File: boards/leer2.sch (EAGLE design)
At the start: 61 parts, among them IC1 XMEGA128A1, IC2 7805DT, Q1 BC846BSMD, Q2 BC846BSMD, Q3 BC846BSMD, Q4 BC846BSMD, Q5 BC846BSMD, Q6 BC846BSMD, Q7 BC846BSMD, Q8 BC846BSMD

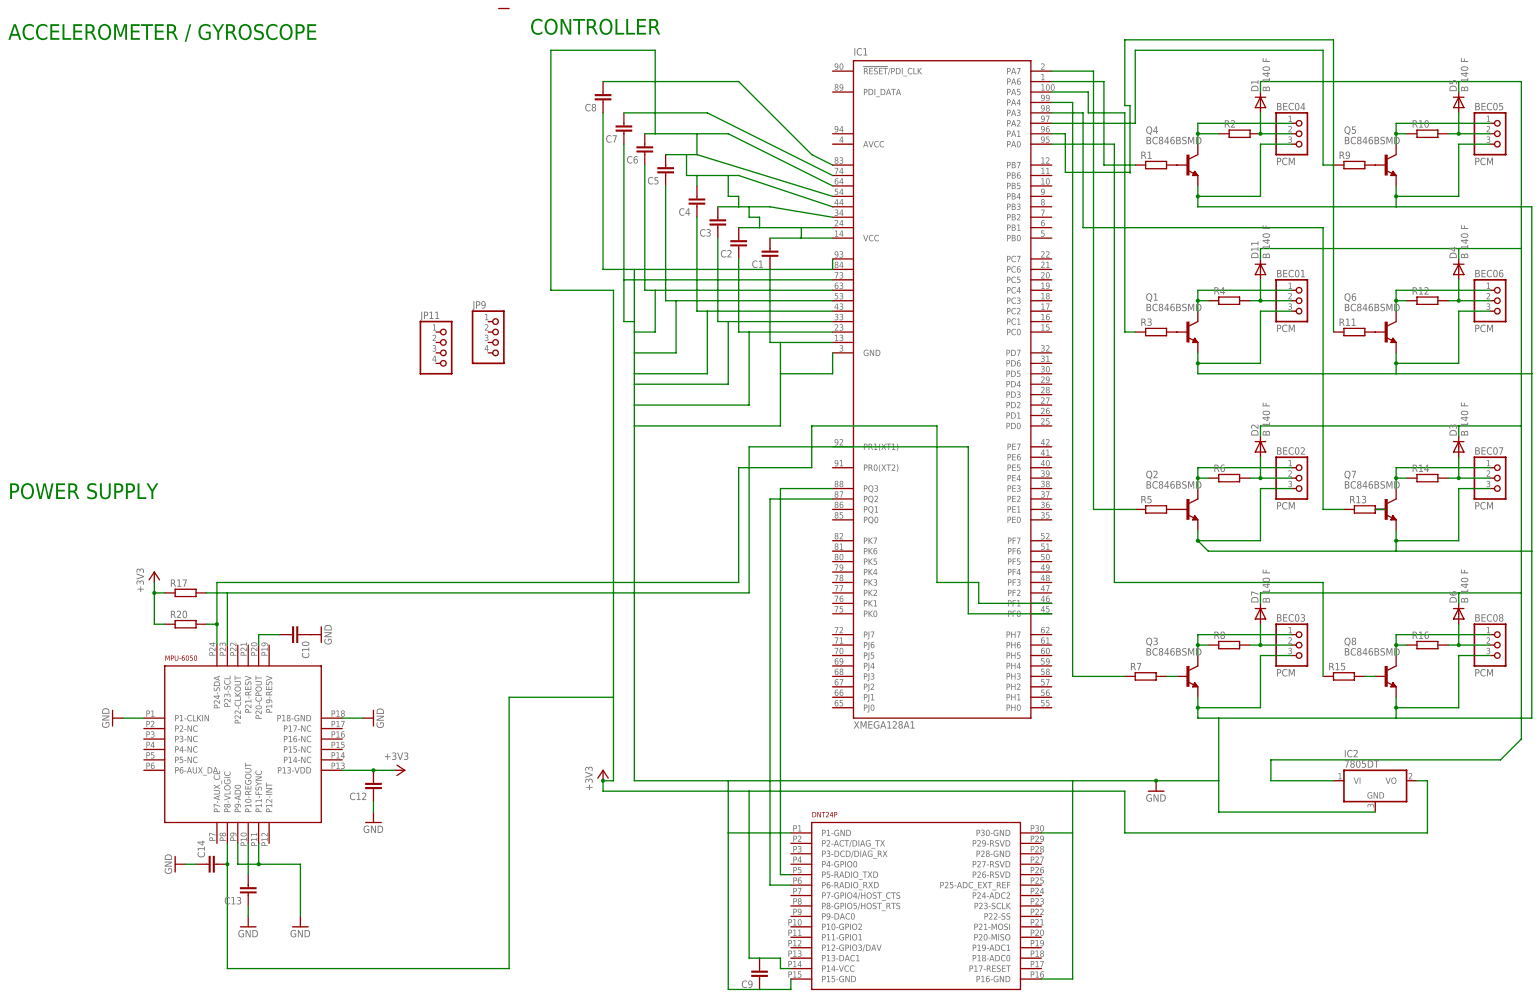
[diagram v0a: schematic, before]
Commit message: - more board changes - we-direkt design rule check modifications - made editable with eagle lite again
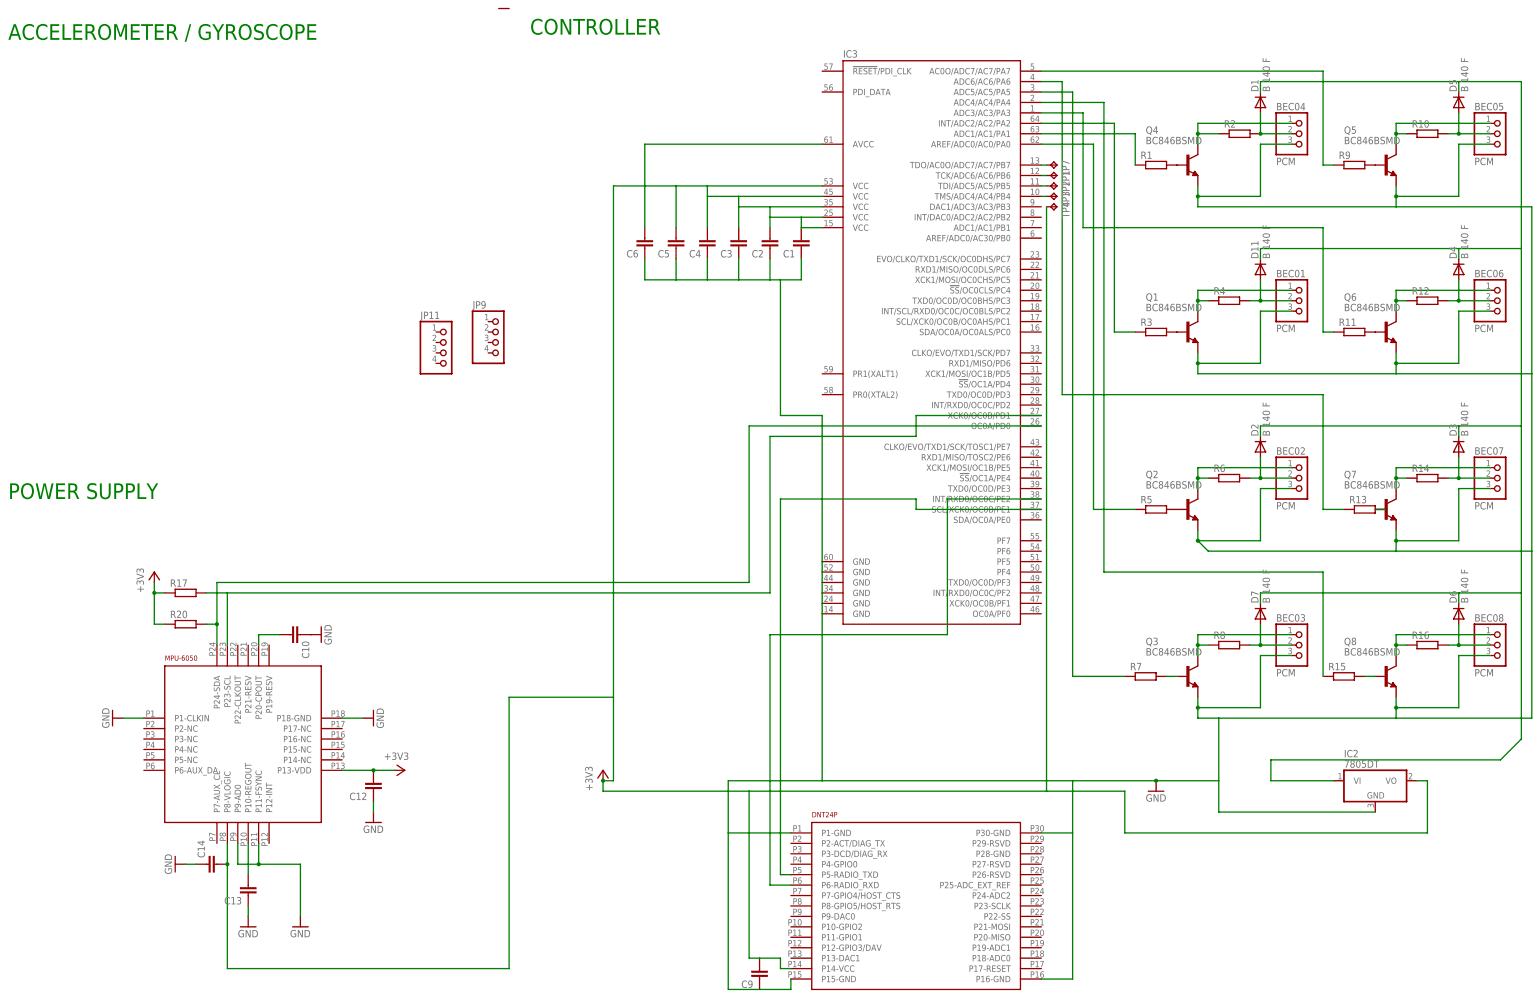
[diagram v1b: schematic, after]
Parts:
- removed C7, C8: (no value), eagle-ltspice:CC0603
- removed IC1: XMEGA128A1, atmel:XMEGA128A1
- added IC3: (no value), ATxmega__A3:ATXMEGA##A3-64A
- added TP1, TP2, TP3, TP4, TP7: TPTP08R, testpad:TPTP08R
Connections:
- new net N$38: IC3.TMS/ADC4/AC4/PB4, TP3.TP
- new net N$39: IC3.TDI/ADC5/AC5/PB5, TP2.TP
- new net N$40: IC3.TCK/ADC6/AC6/PB6, TP1.TP
- new net N$41: IC3.TDO/AC0O/ADC7/AC7/PB7, TP7.TP
- net +3V3: now also IC3.AVCC, IC3.VCC@1, IC3.VCC@2, IC3.VCC@3, IC3.VCC@4, IC3.VCC@5, TP4.TP; no longer C7.2, C8.2, IC1.VCC, IC1.VCC1, IC1.VCC2, IC1.VCC3, IC1.VCC4, IC1.VCC5, IC1.VCC6, IC1.VCC7
- net GND: now also IC3.GND@1, IC3.GND@2, IC3.GND@3, IC3.GND@4, IC3.GND@5, IC3.GND@6; no longer C7.1, C8.1, IC1.GND, IC1.GND1, IC1.GND2, IC1.GND3, IC1.GND4, IC1.GND5, IC1.GND6, IC1.GND7, IC1.GND8, IC1.GND9
- net N$25: now also IC3.ADC1/AC1/PA1; no longer IC1.PA6
- net N$26: now also IC3.INT/ADC2/AC2/PA2; no longer IC1.PA5
- net N$27: now also IC3.AC0O/ADC7/AC7/PA7; no longer IC1.PA2
- net N$28: now also IC3.ADC6/AC6/PA6, R13.1; no longer IC1.PA1, R11.1
- net N$29: now also IC3.AREF/ADC0/AC0/PA0; no longer IC1.PA7
- net N$30: now also IC3.ADC3/AC3/PA3, R11.1; no longer IC1.PA3, R13.1
- net N$31: now also IC3.ADC4/AC4/PA4, R15.1; no longer IC1.PA4, R7.1
- net N$32: now also IC3.ADC5/AC5/PA5, R7.1; no longer IC1.PA0, R15.1
- net N$33: now also IC3.SCL/XCK0/OC0B/PE1; no longer IC1.PQ3
- net N$36: now also IC3.INT/RXD0/OC0C/PE2; no longer IC1.PQ2
- net PF0: now also IC3.OC0A/PD0; no longer IC1.PF1
- net PF1: now also IC3.XCK0/OC0B/PD1; no longer IC1.PF0
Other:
- moved on the sheet: C1, C2, C3, C4, C5, C6
